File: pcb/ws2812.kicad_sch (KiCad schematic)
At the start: 12 parts

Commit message: Parts
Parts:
- D18, D19, D20, D21, D22, D24, D25, DD23: LCSC (none) -> C22371521
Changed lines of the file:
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@@
+			)
+		)
+		(property "LCSC" "C22371521"
+			(at 73.66 111.76 0)
+			(effects
+				(font
+					(size 1.27 1.27)
+				)
+				(hide yes)
 			)
 		)
@@
 			)
 		)
+		(property "LCSC" "C22371521"
+			(at 73.66 96.52 0)
+			(effects
+				(font
+					(size 1.27 1.27)
+				)
+				(hide yes)
+			)
+		)
 		(pin "1"
 		)
@@
 		)
 		(property "Description" ""
+			(at 223.52 96.52 0)
+			(effects
+				(font
+					(size 1.27 1.27)
+				)
+				(hide yes)
+			)
+		)
+		(property "LCSC" "C22371521"
 			(at 223.52 96.52 0)
 			(effects
@@
 			)
 		)
+		(property "LCSC" "C22371521"
+			(at 73.66 66.04 0)
+			(effects
+				(font
+					(size 1.27 1.27)
+				)
+				(hide yes)
+			)
+		)
 		(pin "1"
 		)
@@
 			)
 		)
+		(property "LCSC" "C22371521"
+			(at 223.52 111.76 0)
+			(effects
+				(font
+					(size 1.27 1.27)
+				)
+				(hide yes)
+			)
+		)
 		(pin "1"
 		)
@@
 		)
 		(property "Description" ""
+			(at 223.52 81.28 0)
+			(effects
+				(font
+					(size 1.27 1.27)
+				)
+				(hide yes)
+			)
+		)
+		(property "LCSC" "C22371521"
 			(at 223.52 81.28 0)
 			(effects
@@
 			)
 		)
+		(property "LCSC" "C22371521"
+			(at 73.66 81.28 0)
+			(effects
+				(font
+					(size 1.27 1.27)
+				)
+				(hide yes)
+			)
+		)
 		(pin "1"
 		)
@@
 			(at 223.52 66.04 0)
 			(effects
+				(font
+					(size 1.27 1.27)
+				)
+				(hide yes)
+			)
+		)
+		(property "LCSC" "C22371521"
+			(at 223.52 66.04 0)
+			(effects

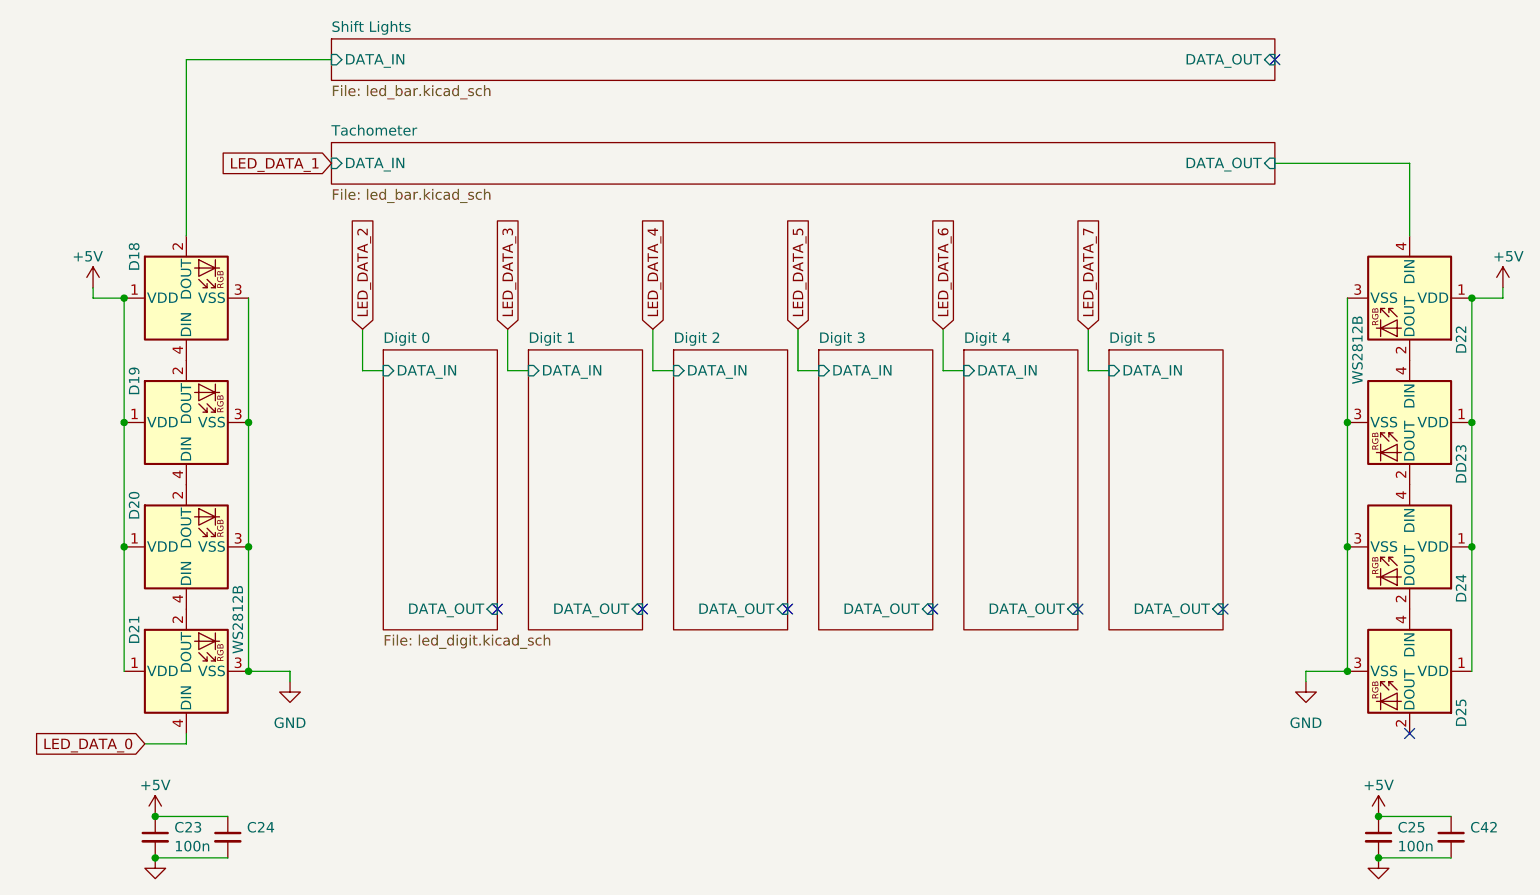
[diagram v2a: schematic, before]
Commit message: LED Footprints fixed
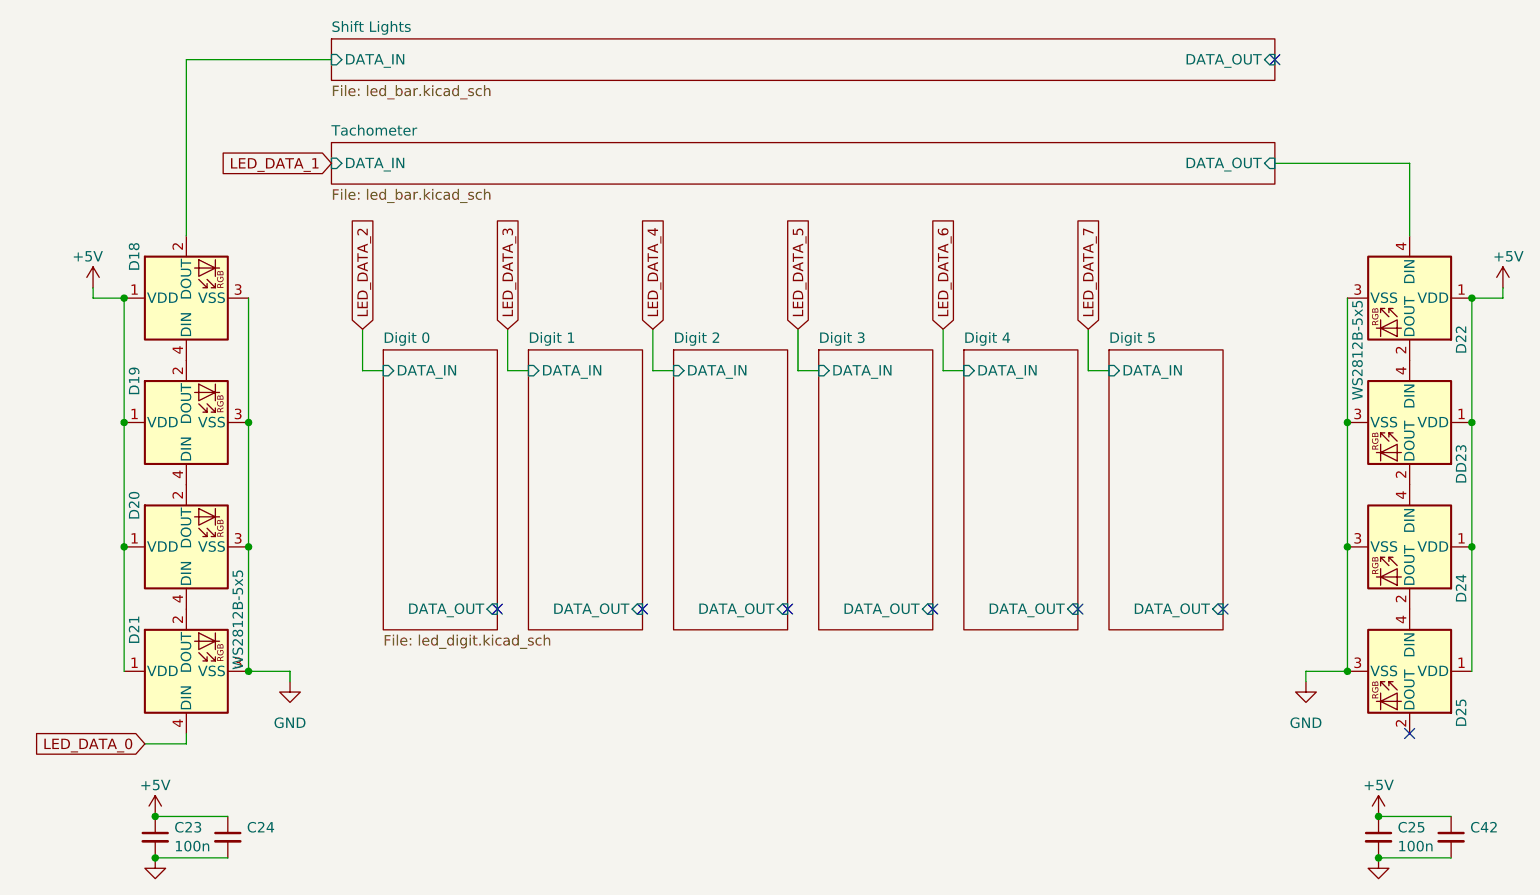
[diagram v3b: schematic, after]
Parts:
- D18, D19, D20, D21, D22, D24, D25, DD23: value WS2812B -> WS2812B-5x5
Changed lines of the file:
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@@
 			)
 		)
-		(property "Value" "WS2812B"
+		(property "Value" "WS2812B-5x5"
 			(at 80.01 105.41 0)
 			(effects
@@
 			)
 		)
-		(property "Value" "WS2812B"
+		(property "Value" "WS2812B-5x5"
 			(at 71.8693 85.09 0)
 			(effects
@@
 			)
 		)
-		(property "Value" "WS2812B"
+		(property "Value" "WS2812B-5x5"
 			(at 225.3107 107.95 0)
 			(effects
@@
 			)
 		)
-		(property "Value" "WS2812B"
+		(property "Value" "WS2812B-5x5"
 			(at 71.8693 54.61 0)
 			(effects
@@
 			)
 		)
-		(property "Value" "WS2812B"
+		(property "Value" "WS2812B-5x5"
 			(at 225.3107 123.19 0)
 			(effects
@@
 			)
 		)
-		(property "Value" "WS2812B"
+		(property "Value" "WS2812B-5x5"
 			(at 217.17 87.63 0)
 			(effects
@@
 			)
 		)
-		(property "Value" "WS2812B"
+		(property "Value" "WS2812B-5x5"
 			(at 71.8693 69.85 0)
 			(effects
@@
 			)
 		)
-		(property "Value" "WS2812B"
+		(property "Value" "WS2812B-5x5"
 			(at 217.17 72.39 0)
 			(effects
